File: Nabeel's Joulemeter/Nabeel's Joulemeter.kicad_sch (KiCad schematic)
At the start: 3 parts, among them J1 XT60-M, J2 XT60-M, U1 INA181A1QDBVRQ1

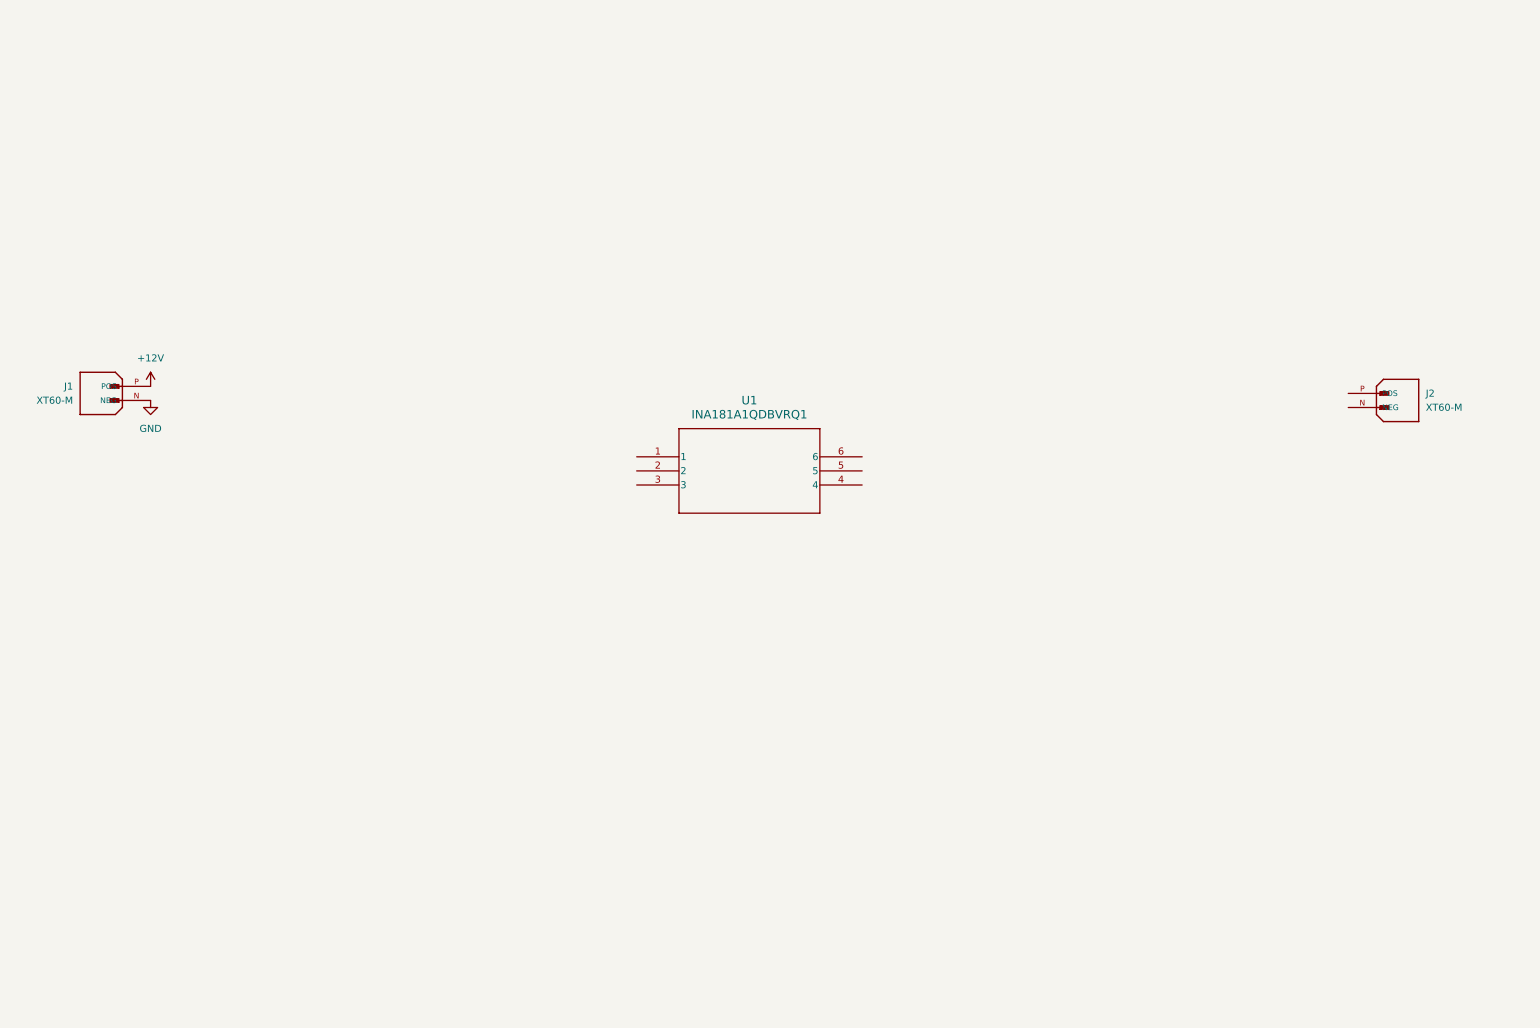
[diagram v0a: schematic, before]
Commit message: more progress so far on schematic
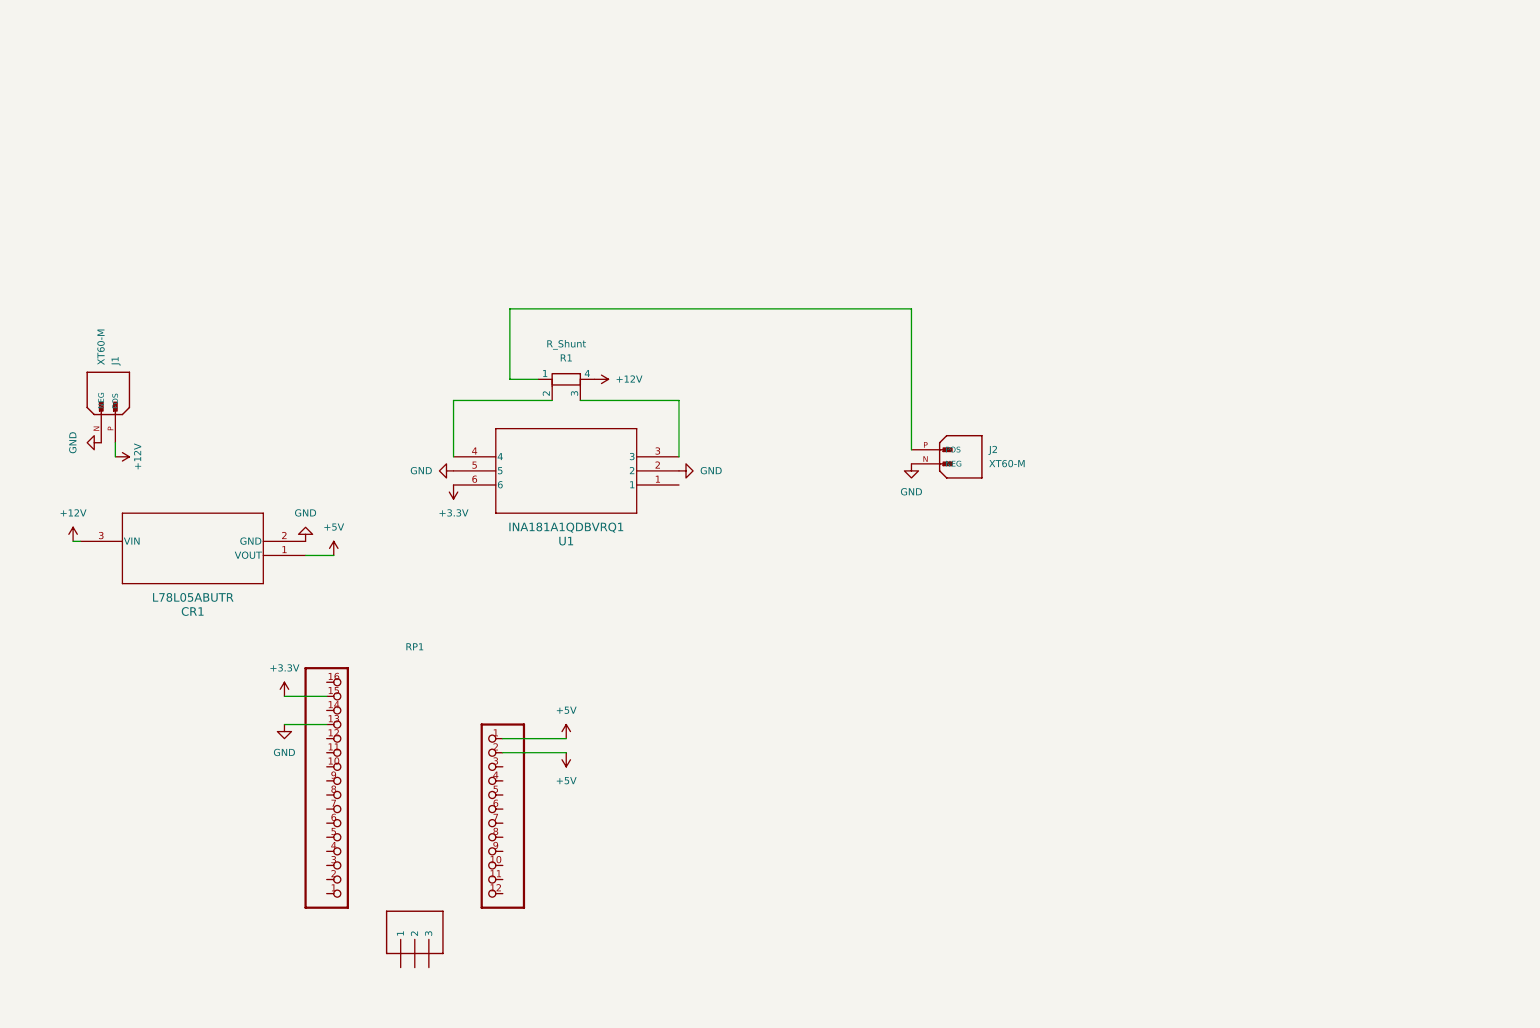
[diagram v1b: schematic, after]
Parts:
- added CR1: L78L05ABUTR, SOT-89_STM, symbol SMV_Custom:L78L05ABUTR
- added R1: R_Shunt, symbol Device:R_Shunt
- added RP1: ~, symbol SMV_Custom:RP2040
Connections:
- net +12V: now also CR1.3 (VIN), R1.4
- net GND: now also J2.N (NEG), U1.2, U1.5, CR1.2 (GND), RP1.13
- net at U1.3: now also R1.3
- net at U1.4: now also R1.2
- net +3.3V: now reaches U1.6
- net +3.3V: now also RP1.15
- net at J2.P (POS): now also R1.1
- new net +5V: CR1.1 (VOUT), RP1.1, RP1.2
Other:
- moved on the sheet: J1, J2, U1

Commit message: rough draft of schematic done
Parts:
- added J3: 22035035, CON_22035035_MOL, symbol SMV_Custom:3-pin Mini Molex Spox
- added R2: R, CRCW080510K0FKEAC:RESC2012X60N, symbol Device:R
- added R3: R, symbol Device:R
- added U2: PADS131M04QPWRQ1, TSSOP20_PW_TEX, symbol SMV_Custom:PADS131M04QPWRQ1
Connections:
- net +3.3V: now also U2.1 (AVDD), U2.20 (DVDD)
- net +5V: now also RP1.3; no longer RP1.1, RP1.2
- net GND: now also R3.2, U2.19 (DGND), U2.2 (AGND), U2.4 (AIN0N), U2.5 (AIN1N)
- net AMPLIFIED_VOLTAGE: now reaches U1.1
- net AMPLIFIED_VOLTAGE: now also U2.3 (AIN0P)
- net SHUNT_TO_LOAD: now reaches J2.P (POS), R1.1
- net SHUNT_TO_LOAD: now also R2.1
- net ADC_TO_RP: now reaches RP1.10
- net ADC_TO_RP: now also U2.15 (DOUT)
- new net DIVIDED_VOLTAGE: R2.2, R3.1, U2.6 (AIN1P)
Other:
- note added: "ADC"
- note added: "Can Bus Thing (I think)"
- note added: "Current Sensing Chip & Shunt Resistor"
- note added: "LDO"
- note added: "Raspberry Pi"
- note added: "Voltage Divider"
- moved on the sheet: J1, J2, R1, RP1, U1

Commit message: some revisions to board
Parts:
- removed CR1: L78L05ABUTR, SOT-89_STM, symbol SMV_Custom:L78L05ABUTR
- removed R2: R, CRCW080510K0FKEAC:RESC2012X60N, symbol Device:R
- removed R3: R, symbol Device:R
- added C1, C3, C6: 0.1uF,50V, SMV_Passives:Cap0805, symbol SMV_Custom:C0805C104K5RACTU
- added C2: 0.33uF,50V, SMV_Passives:Cap0805, symbol SMV_Custom:C0805C334K5RACTU
- added C4, C5: 1uF,16V, SMV_Passives:Cap0805, symbol SMV_Custom:C0805C105K4RACTU
- added R4: RS73F2BTTD1005D, 10MOhms, RS73F2BTTD1005D:RESC3216X70N, symbol SMV_Custom:RS73F2BTTD1005D
- added R5: CRCW04022M00FKED, 2MOhms, RES_CRCW_0402, symbol SMV_Custom:CRCW04022M00FKED
- added U3: UA78M05QDCYRG4Q1, SMV_ICs:DCY4_TEX, symbol SMV_Custom:UA78M05QDCYRG4Q1
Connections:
- net +12V: now also C2.1, U3.3 (INPUT)
- net +3.3V: now also C3.1, C4.1, C5.1
- net +5V: now also C1.1, C6.1, U3.1 (OUTPUT)
- net DIVIDED_VOLTAGE: now also R4.1, R5.2
- net GND: now also C1.2, C2.2, C3.2, C4.2, C5.2, C6.2, R5.1, U3.2 (GND), U3.4 (GND)
- net SHUNT_TO_LOAD: now also R4.2
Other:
- moved on the sheet: J2, R1, RP1, U1, U2

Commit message: my board after grinding some more
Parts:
- removed C6: 0.1uF,50V, SMV_Passives:Cap0805, symbol SMV_Custom:C0805C104K5RACTU
- removed R4: RS73F2BTTD1005D, 10MOhms, RS73F2BTTD1005D:RESC3216X70N, symbol SMV_Custom:RS73F2BTTD1005D
- removed R5: CRCW04022M00FKED, 2MOhms, RES_CRCW_0402, symbol SMV_Custom:CRCW04022M00FKED
- added C6: GCM188R71H104KA57D, 220nF, SMV_Passives:0805RESC2012X60N, symbol SMV_Custom:GCM188R71H104KA57D
- added C7: 0.1uF,50V, SMV_Passives:Cap0805, symbol SMV_Custom:C0805C104K5RACTU
- added C8, C9: C1808C472KGRACTU, 4700pF, CAPC520220_215N_KEM, symbol SMV_Custom:C1808C472KGRACTU
- added R2: 10k, SMV_Passives:0805RESC2012X60N, symbol SMV_Custom:CRCW080510K0FKEAC
- added R3: TNPW0805505KBEEA, TNPW0805505KBEEA:RESC2012X55N, symbol SMV_Custom:TNPW0805505KBEEA
- added R4: TNPW0805101KBEEA, TNPW0805101KBEEA:RESC2012X55N, symbol SMV_Custom:TNPW0805101KBEEA
- added R5, R6: CRCW020149R9FNED, 50Ω, SMV_Passives:0805RESC2012X60N, symbol SMV_Custom:CRCW020149R9FNED
- added U4: MCP6286T-E/OT, SMV_ICs:SOT-23-5_MC_MCH, symbol SMV_Custom:MCP6286T-E_OT
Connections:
- net ADC_TO_RP is gone; now on net MISO: RP1.10, U2.15 (DOUT)
- net +3.3V: now also C7.1, R2.1, U4.5 (VDD)
- net AMPLIFIED_VOLTAGE: now also C9.2, R6.1; no longer U1.1
- net DIVIDED_VOLTAGE: now also C8.2, R5.1
- net GND: now also C6.2, C7.2, C8.1, C9.1, R4.1, U4.2 (VSS)
- net SHUNT_TO_LOAD: now also R3.2
- net GPIO_RESET: now reaches U2.11 (SYNC/RESET)
- net GPIO_RESET: now also RP1.7
- net CS: now reaches U2.12 (CS)
- net CS: now also RP1.9, R2.2
- net SCK: now reaches U2.14 (SCLK)
- net SCK: now also RP1.12
- net MOSI: now reaches U2.16 (DIN)
- net MOSI: now also RP1.11
- net GPIO_CLKIN: now reaches U2.17 (CLKIN)
- net GPIO_CLKIN: now also RP1.8
- net at U2.18 (CAP): now also C6.1
- net MISO: now reaches RP1.10
- new net: R3.1, R4.2, U4.3 (VIN+)
- new net: R6.2, U1.1
- new net FEEDBACK: R5.2, U4.1 (VOUT), U4.4 (VIN-)
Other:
- note added: "Current Sensing"
- note added: "Voltage Divider -> OP Amp -> RC Filter"
- note removed: "Current Sensing Chip & Shunt Resistor"
- note removed: "Voltage Divider"
- moved on the sheet: C1, C2, C3, C4, C5, J1, J2, R1, RP1, U1, U2, U3

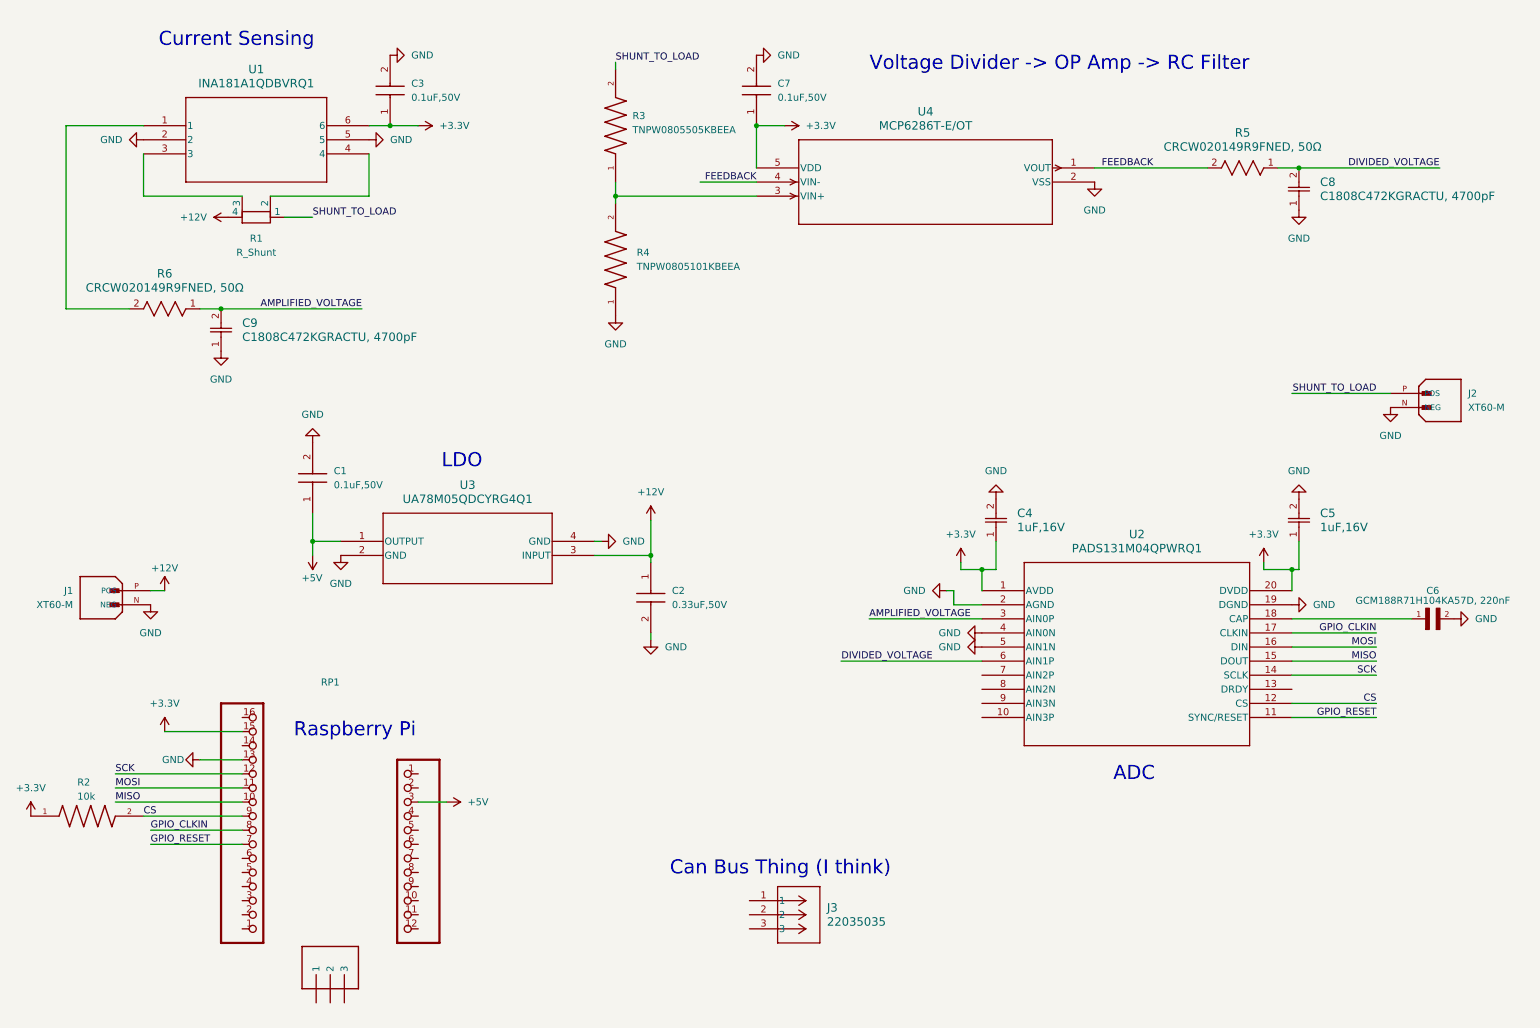
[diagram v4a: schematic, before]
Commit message: completed schematic except test points and leds
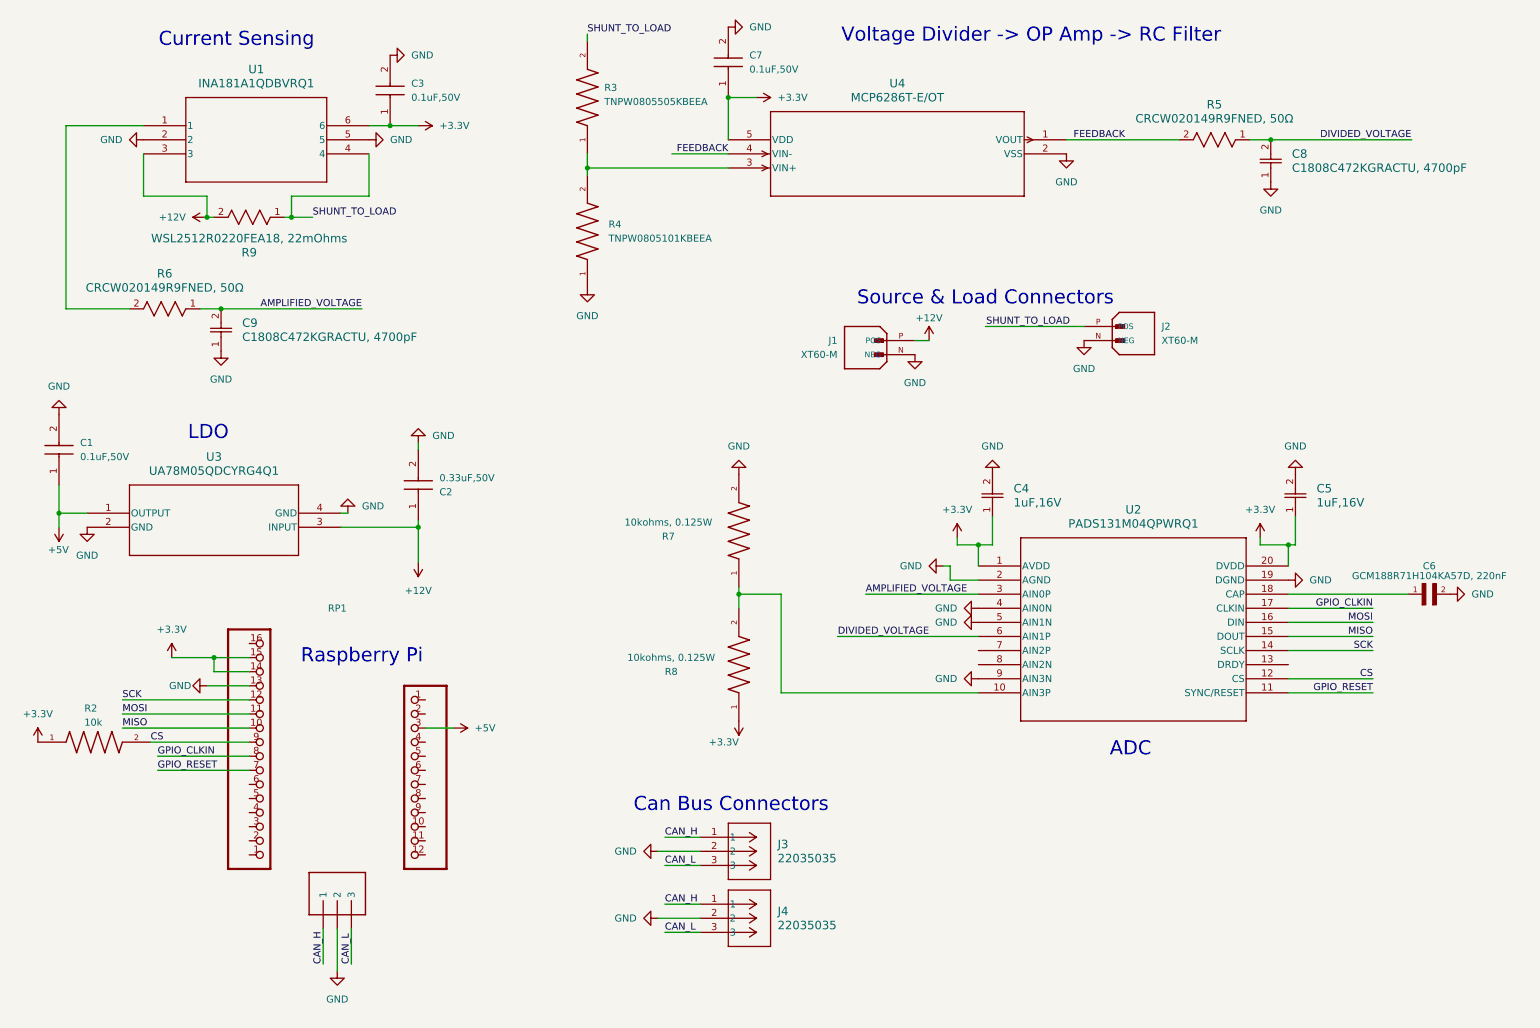
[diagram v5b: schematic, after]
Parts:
- removed R1: R_Shunt, symbol Device:R_Shunt
- added J4: 22035035, CON_22035035_MOL, symbol SMV_Custom:3-pin Mini Molex Spox
- added R7, R8: 10kohms, 0.125W, SMV_Passives:0805RESC2012X60N, symbol SMV_Custom:CRCW080510K0FKEAC
- added R9: WSL2512R0220FEA18, 22mOhms, WSL2512_VIS, symbol SMV_Custom:WSL2512R0220FEA18
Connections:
- net +12V: now also U1.3, R9.2
- net +3.3V: now also RP1.14, R8.1
- net GND: now also J3.2, RP1.2, U2.9 (AIN3N), J4.2, R7.2
- net SHUNT_TO_LOAD: now also U1.4, R9.1
- net at U2.10 (AIN3P): now also R7.1, R8.2
- net CAN_H: now reaches J3.1
- net CAN_H: now also RP1.1, J4.1
- net CAN_L: now reaches J3.3
- net CAN_L: now also RP1.3, J4.3
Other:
- note added: "Can Bus Connectors"
- note added: "Source & Load Connectors"
- note removed: "Can Bus Thing (I think)"
- moved on the sheet: C1, C2, C4, C5, C6, C7, C8, J1, J2, J3, R2, R3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

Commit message: RAHHHHH FINISHED MY SCHEMATIC
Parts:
- removed R9: WSL2512R0220FEA18, 22mOhms, WSL2512_VIS, symbol SMV_Custom:WSL2512R0220FEA18
- added D1, D2, D3: WL-SMCW_0603, SMV_Passives:WL-SMCW_0603(diode), symbol SMV_Custom:WL-SMCW_0603
- added R1: WSR5R0100FEA, 10mOhms, WSR, symbol SMV_Custom:WSR5R0100FEA
- added R10, R11, R9: RCS0603150RJNEA, 150Ω, SMV_Passives:0805RESC2012X60N, symbol SMV_Custom:RCS0603150RJNEA
- added TP1, TP10, TP11, TP12, TP13, TP14, TP15, TP16, TP17, TP2, TP3, TP4, TP5, TP6, TP7, TP8, TP9: TestPoint, symbol Connector:TestPoint
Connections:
- net +12V: now also R1.1, TP1.1
- net +3.3V: now also R9.2, TP3.1
- net +5V: now also TP4.1
- net AMPLIFIED_VOLTAGE: now also TP17.1
- net CAN_H: now also TP16.1
- net CAN_L: now also TP15.1
- net CS: now also TP9.1
- net DIVIDED_VOLTAGE: now also TP12.1
- net FEEDBACK: now also TP11.1
- net GND: now also D1.1, D2.1, D3.1, TP13.1
- net GPIO_CLKIN: now also TP5.1
- net GPIO_RESET: now also TP10.1
- net MISO: now also TP7.1
- net MOSI: now also TP6.1
- net SCK: now also TP8.1
- net SHUNT_TO_LOAD: now also R1.2, TP2.1
- net at R3.1, R4.2, U4.3 (VIN+): now also TP14.1
- new net: D3.2, R11.1
- new net: R11.2, RP1.2
- new net: D2.2, R10.1
- new net: R10.2, RP1.1
- new net: D1.2, R9.1
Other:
- moved on the sheet: C1, C2, C3, C4, C5, C6, C7, C8, C9, J1, J2, J3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

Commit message: pcb layout progress on jan 22
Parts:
- removed C2: 0.33uF,50V, SMV_Passives:Cap0805, symbol SMV_Custom:C0805C334K5RACTU
- removed C9: C1808C472KGRACTU, 4700pF, CAPC520220_215N_KEM, symbol SMV_Custom:C1808C472KGRACTU
- added C10: C1210C474K5RACTU, 0.47uF, SMV_Passives:CAPC340270_105N_KEM, symbol SMV_Custom:C1210C474K5RACTU
- added C2: C0603C472K4RACTU, 4700pF, SMV_Passives:CAPC17595_87N_KEM, symbol SMV_Custom:C0603C472K4RACTU
- added TP18: TestPoint, TestPoint:TestPoint_Pad_D2.0mm, symbol Connector:TestPoint
- J1, J2: footprint XT60-M:AMASS_XT60-M -> SMV_Connectors:AMASS_XT60-M
- J3, J4: footprint CON_22035035_MOL -> SMV_Connectors:3pin_CON_22035035_MOL
- R3: footprint TNPW0805505KBEEA:RESC2012X55N -> SMV_Passives:RESC2012X55N
- R4: footprint TNPW0805101KBEEA:RESC2012X55N -> SMV_Passives:RESC2012X55N
- RP1: footprint (none) -> SMV_Connectors:RP2040
- TP1, TP10, TP11, TP12, TP13, TP14, TP15, TP16, TP17, TP2, TP3, TP4, TP5, TP6, TP7, TP8, TP9: footprint (none) -> TestPoint:TestPoint_Pad_D2.0mm
- U1: footprint SOIC_DBVRQ1_TEX -> SMV_ICs:SOIC_DBVRQ1_TEX
- U2: footprint TSSOP20_PW_TEX -> SMV_ICs:TSSOP20_PW_TEX
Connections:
- net +12V: now also C10.1
- net +3.3V: now also RP1.26 (3.3V), RP1.27 (3.3V); no longer RP1.14, RP1.15
- net AMPLIFIED_VOLTAGE: now also C2.2
- net CAN_H: now also RP1.31 (CAN_H); no longer RP1.1
- net CAN_L: now also RP1.29 (CAN_L); no longer RP1.3
- net CS: now also RP1.21 (A3); no longer RP1.9
- net GND: now also RP1.25 (GND), RP1.30 (GND), U2.7 (AIN2P), U2.8 (AIN2N), C10.2, C2.1; no longer RP1.13, RP1.2
- net GPIO_CLKIN: now also RP1.24 (A0); no longer RP1.8
- net GPIO_RESET: now also RP1.20 (D24); no longer RP1.7
- net MISO: now also RP1.22 (A2); no longer RP1.10
- net MOSI: now also RP1.23 (A1); no longer RP1.11
- net SCK: now also RP1.18 (SCK); no longer RP1.12
- net at R11.2: now also RP1.14 (TX); no longer RP1.2
- net at R6.2, U1.1: now also TP18.1
- net at R10.2: now also RP1.13 (D4); no longer RP1.1
- no-connect marks 0 -> 17
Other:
- moved on the sheet: D1, D2, D3, R10, R11, R2, R9, TP15, TP16, TP3

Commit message: latest schematic and pcb draft
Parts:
- removed J1, J2: XT60-M, SMV_Connectors:AMASS_XT60-M, symbol SMV_Custom:XT60-M
- added C11, C9: 470uF, 63V, SMV_Passives:Big_Chunky_Cap, symbol SMV_Custom:Big_Chunky_Cap2
- added J1, J5: 430450200, SMV_Connectors:CONN_SD-43045-001_02_MOL, symbol SMV_Custom:430450200
- added R12, R13: R_US, Resistor_THT:R_Axial_DIN0204_L3.6mm_D1.6mm_P1.90mm_Vertical, symbol Device:R_US
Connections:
- net +12V: now also C11.1, J5.1
- net GND: now also J1.2, J5.2, R12.2, R13.2
- net SHUNT_TO_LOAD: now also C9.2, J1.1
- new net: C11.2, R12.1
- new net: C9.1, R13.1
